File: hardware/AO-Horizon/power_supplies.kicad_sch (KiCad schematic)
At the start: 0 parts

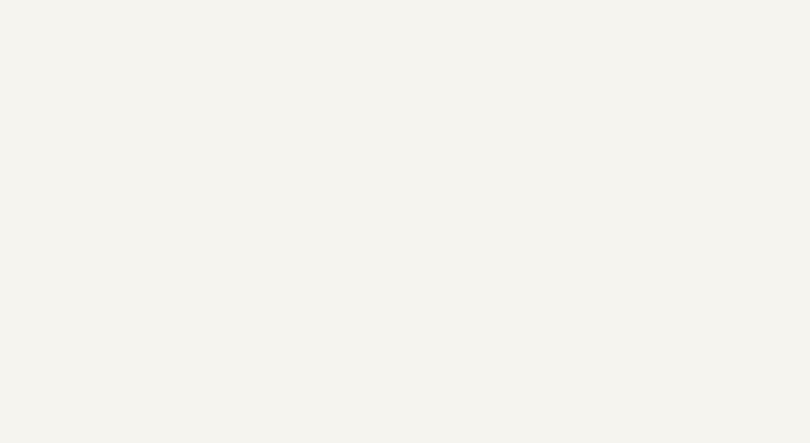
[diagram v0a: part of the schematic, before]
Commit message: feat(hardware): add project library, lib tables and design records (#4)
* docs(readme): simplify workflow diagram explanation

Mark DRAFT as under review, sync CHECK label, and add a colour key in README and template.

Co-Authored-By: Claude Sonnet 5.5 <noreply@anthropic.com>

* Update settings.json

* change spec file name

* update git-workflow skill

* change skill name by add hw-*

* docs: update AeroOptix-Horizon hardware spec

* docs: consolidate hardware handoff into checklist

* Update CLAUDE.md

* Update CLAUDE.md

* Update CLAUDE.md

* feat(hooks): replace protect hook with rule-based v2

Move file-protection rules into hooks/protect.json (allow > deny > ask)
and use ask for editable-with-approval files instead of a hard block.
Bash/PowerShell checks now inspect write targets, not any mention of a
protected path. Align settings.json permissions and drop the old hook.

Co-Authored-By: Claude Sonnet 5.5 <noreply@anthropic.com>

* docs: update CLAUDE.md for protection tiers and skill names

Describe the ask/deny protection rules, the v2 hook and protect.json,
and fix stale skill and template names.

Co-Authored-By: Claude Sonnet 5.5 <noreply@anthropic.com>

* Update .gitignore

* Update .gitignore

* Update .gitignore

* del skills

* Update engineering.md

* Update git-workflow.md

* Update hardware-workflow.md

* Update settings.json

* Update pull_request_template.md

* Update .gitignore

* Update .gitignore

* Delete SKILL.md

* Delete SKILL.md

* Update .gitignore

* add git-workflow skill

* Update CLAUDE.md

* Update protect.json

* Update settings.json

* Create MEMORY.md

* feat(agents): add codex-hw-delegate for bounded Codex tasks

Add a project agent that delegates one small, read-only-by-default task
to Codex CLI. It gates trivial or ambiguous requests, refuses PDF and
KiCad file contents, never mutates git, cross-checks Codex output and
returns a fixed report format.

Co-Authored-By: Claude Sonnet 5.5 <noreply@anthropic.com>

* fix(hooks): resol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
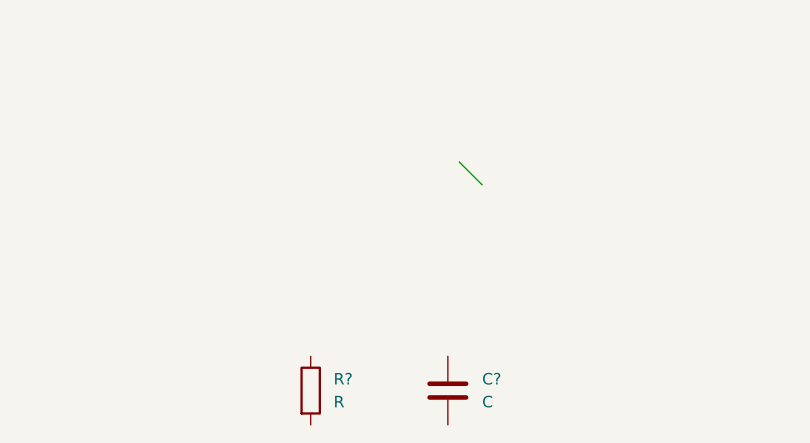
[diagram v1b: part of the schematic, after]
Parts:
- added C?: C, 0_Capacitor_SMD:C_0603_1608Metric_NomDensity, symbol Device:C
- added R?: R, 0_Resistor_SMD:R_0402_1005Metric_NomDensity, symbol Device:R
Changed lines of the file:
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@@
+		)
+	)
+	(bus_entry
+		(at 219.71 125.73)
+		(size 2.54 2.54)
+		(stroke
+			(width 0)
+			(type default)
+		)
+	)
+	(symbol
+		(lib_id "Device:C")
+		(at 218.44 151.13 0)
+		(unit 1)
+		(body_style 1)
+		(exclude_from_sim no)
+		(in_bom yes)
+		(on_board yes)
+		(in_pos_files yes)
+		(dnp no)
+		(fields_autoplaced yes)
+		(property "Reference" "C?"
+			(at 222.25 149.86 0)
+			(show_name no)
+			(do_not_autoplace no)
+			(effects
+				(font
+					(size 1.27 1.27)
+				)
+				(justify left)
+			)
+		)
+		(property "Value" "C"
+			(at 222.25 152.4 0)
+			(show_name no)
+			(do_not_autoplace no)
+			(effects
+				(font
+					(size 1.27 1.27)
+				)
+				(justify left)
+			)
+		)
+		(property "Footprint" "0_Capacitor_SMD:C_0603_1608Metric_NomDensity"
+			(at 219.4052 154.94 0)
+			(hide yes)
+			(show_name no)
+			(do_not_autoplace no)
+			(effects
+				(font
+					(size 1.27 1.27)
+				)
+			)
+		)
+		(property "Datasheet" ""
+			(at 218.44 151.13 0)
+			(hide yes)
+			(show_name no)
+			(do_not_autoplace no)
+			(effects
+				(font
+					(size 1.27 1.27)
+				)
+			)
+		)
+		(property "Description" "Unpolarized capacitor"
+			(at 218.44 151.13 0)
+			(hide yes)
+			(show_name no)
+			(do_not_autoplace no)
+			(effects
+				(font
+					(size 1.27 1.27)
+				)
+			)
+		)
+		(pin "1"
+		)
+		(pin "2"
+		)
+		(instances
+			(project "AO-Horizon"
+				(path "/76162bf1-0d95-48cb-b65a-4de551455d04/85f6b8f0-e85e-4d9f-8681-ac148f93be5a/5920cc04-6cd8-462c-b523-fb850d762b0c"
+					(reference "C?")
+					(unit 1)
+				)
+			)
+		)
+	)
+	(symbol
+		(lib_id "Device:R")
+		(at 203.2 151.13 0)
+		(unit 1)
+		(body_style 1)
+		(exclude_from_sim no)
+		(in_bom yes)
+		(on_board yes)
+		(in_pos_files yes)
+		(dnp no)
+		(fields_autoplaced yes)
+		(property "Reference" "R?"
+			(at 205.74 149.86 0)
+			(show_name no)
+			(do_not_autoplace no)
+			(effects
+				(font
+					(size 1.27 1.27)
+				)
+				(justify left)
+			)
+		)
+		(property "Value" "R"
+			(at 205.74 152.4 0)
+			(show_name no)
+			(do_not_autoplace no)
+			(effects
+				(font
+					(size 1.27 1.27)
+				)
+				(justify left)
+			)
+		)
+		(property "Footprint" "0_Resistor_SMD:R_0402_1005Metric_NomDensity"
+			(at 201.422 151.13 90)
+			(hide yes)
+			(show_name no)
+			(do_not_autoplace no)
+			(effects
+				(font
+					(size 1.27 1.27)
+				)
+			)
+		)
+		(property "Datasheet" ""
+			(at 203.2 151.13 0)
+			(hide yes)
+			(show_name no)
+			(do_not_autoplace no)
+			(effects
+				(font
+					(size 1.27 1.27)
+				)
+			)
+		)
+		(property "Description" "Resistor"
+			(at 203.2 151.13 0)
+			(hide yes)
+			(show_name no)
+			(do_not_autoplace no)
+			(effects
+				(font
+					(size 1.27 1.27)
+				)
+			)
+		)
+		(pin "2"
+		)
+		(pin "1"
+		)
+		(instances
+			(project "AO-Horizon"
+				(path "/76162bf1-0d95-48cb-b65a-4de551455d04/85f6b8f0-e85e-4d9f-8681-ac148f93be5a/5920cc04-6cd8-462c-b523-fb850d762b0c"
+					(reference "R?")
+					(unit 1)
+				)
+			)
 		)
 	)

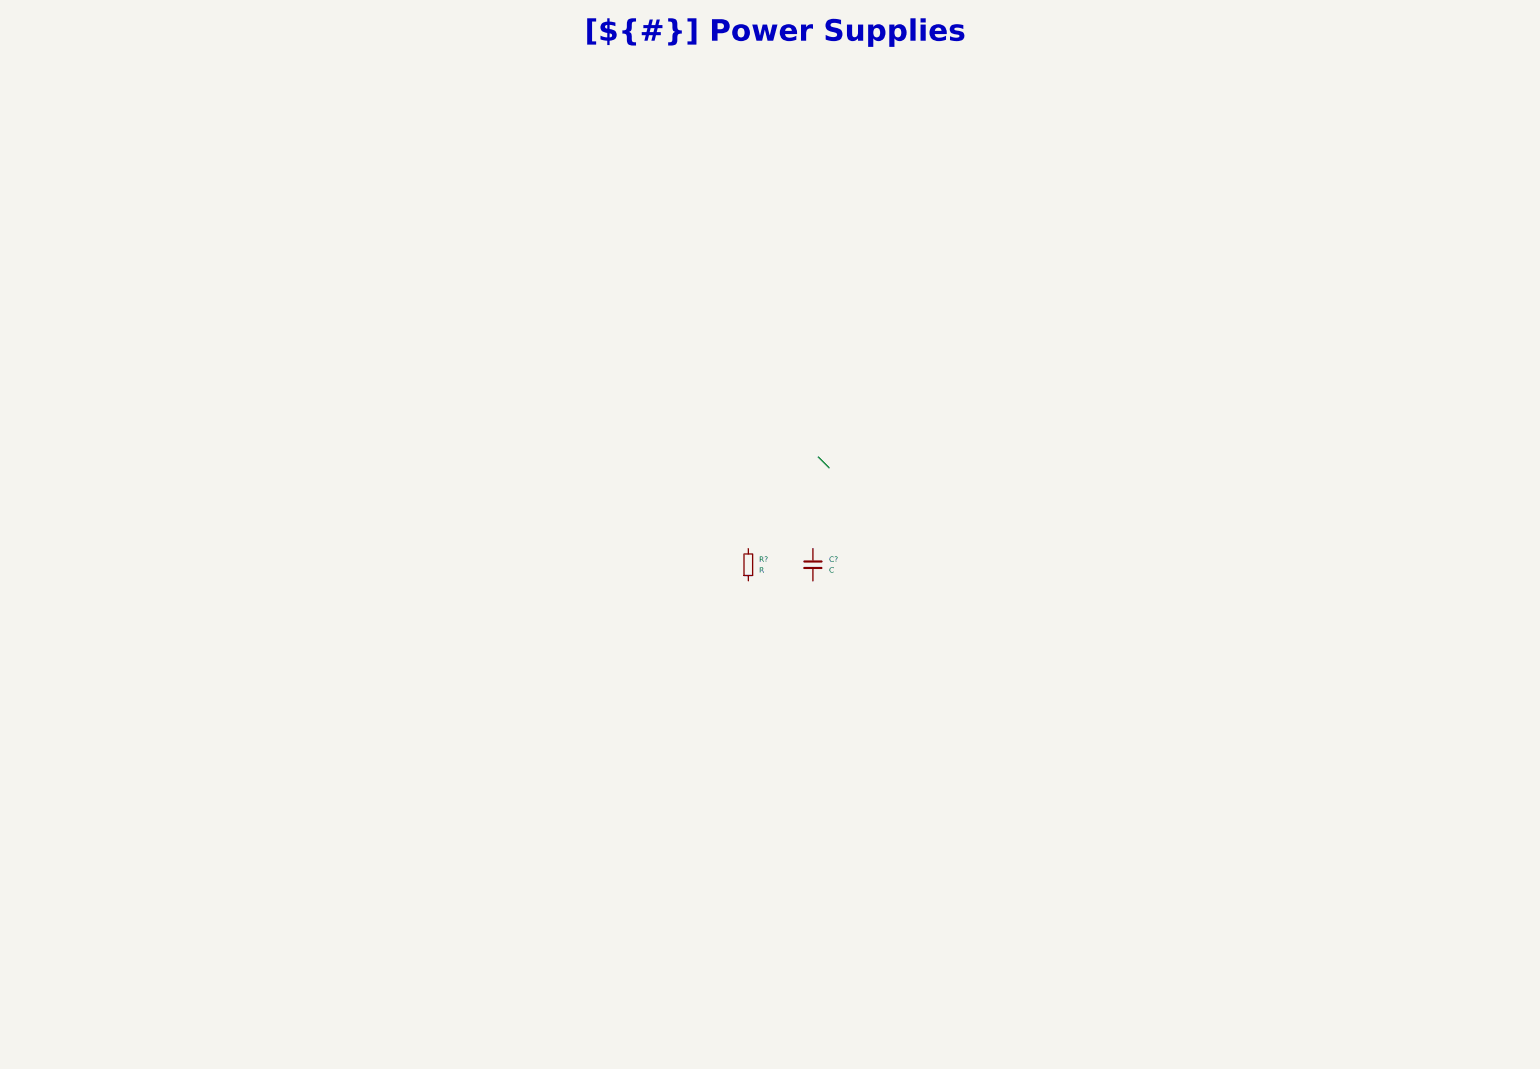
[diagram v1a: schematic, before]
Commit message: feat(power): add TPS62142 3V3 buck and power sheet parts
- power_supplies.kicad_sch: add TPS62142 buck (5V to 3V3) with inductor,
  capacitors and LED, TPS73533DRB LDO (+3.3VA), DF2S6.2CT ESD and a
  6-pin input connector.
- Add the new local libraries to fp-lib-table and sym-lib-table.
- Update AO-Horizon.kicad_sch (embedded font), block_diagram.kicad_sch
  and project settings.

ERC/DRC: NOT_VERIFIED.

Co-Authored-By: Claude Opus 5.5 <noreply@anthropic.com>
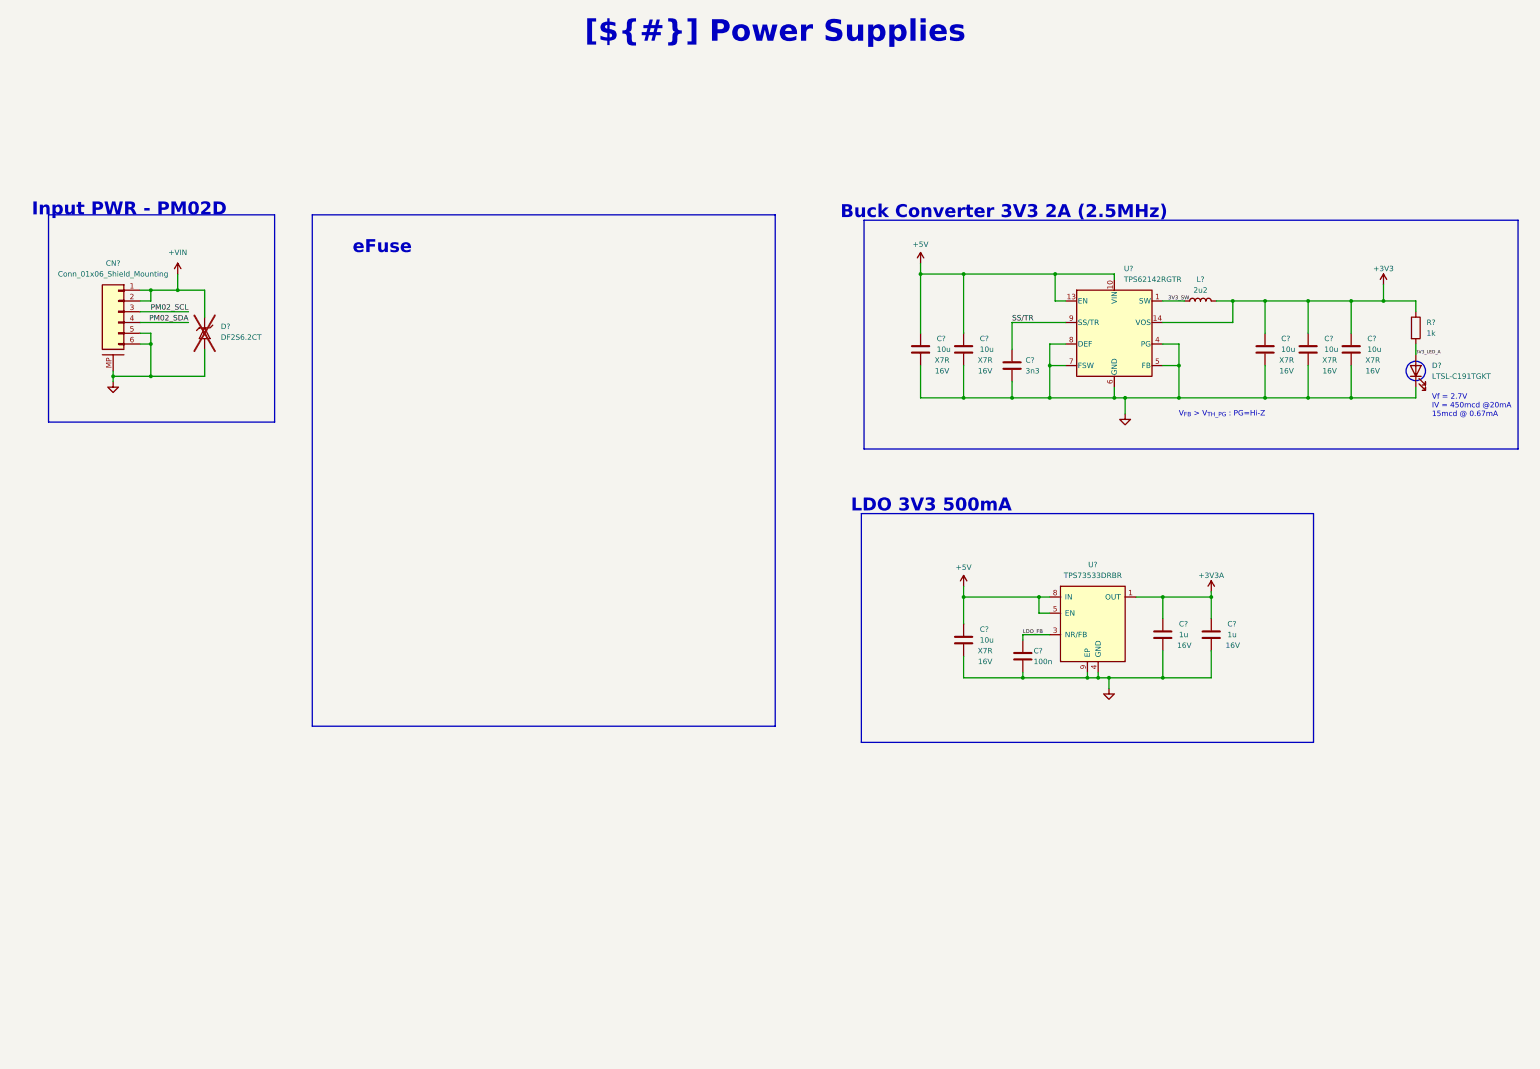
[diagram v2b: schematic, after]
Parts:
- removed C?: C, 0_Capacitor_SMD:C_0603_1608Metric_NomDensity, symbol Device:C
- removed R?: R, 0_Resistor_SMD:R_0402_1005Metric_NomDensity, symbol Device:R
- added C? (x2): 1u, 0_Capacitor_SMD:C_0603_1608Metric_NomDensity, symbol Device:C
- added C? (x6): 10u, 0_Capacitor_SMD:C_0805_2012Metric_NomDensity, symbol Device:C
- added C?: 3n3, 0_Capacitor_SMD:C_0603_1608Metric_NomDensity, symbol Device:C
- added C?: 100n, 0_Capacitor_SMD:C_0603_1608Metric_NomDensity, symbol Device:C
- added CN?: Conn_01x06_Shield_Mounting, 0_Conn_JST:JST_GH_SM06B-GHS-TB_1x06-1MP_P1.25mm_Horizontal, symbol 0_Conn_Generic:Conn_01x06_MountingPin
- added D?: LTSL-C191TGKT, 0_LED_SMD:LED_0603_1608Metric, symbol Device:LED
- added D?: DF2S6.2CT, 0_Diode_SMD:D_SOD-882, symbol 0_Protection_ESD:DF2S6.2CT
- added L?: 2u2, 0_Inductor_SMD:L_Abracon_AOTA-B252010S, symbol Device:L
- added R?: 1k, 0_Resistor_SMD:R_0603_1608Metric_NomDensity, symbol Device:R
- added U?: TPS73533DRBR, 0_Package_SON:VSON-8-1EP_3x3mm_P0.65mm__EP1.5x1.75mm_ThermalVias_DRV8601DRBT, symbol 0_Regulator_Linear:TPS73533DRB
- added U?: TPS62142RGTR, 0_Package_DFN_QFN:VQFN-16-1EP_3x3mm_P0.5mm_EP1.68x1.68mm_ThermalVias, symbol 0_Regulator_Switching:TPS62142
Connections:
- new net +3V3: C?.1, C?.1, C?.1, L?.2, R?.1, U?.14 (VOS)
- new net +3V3A: C?.1, C?.1, U?.1 (OUT)
- new net +5V: C?.1, C?.1, C?.1, U?.10 (VIN), U?.11 (VIN), U?.12 (VIN), U?.13 (EN), U?.5 (EN), U?.8 (IN)
- new net +VIN: CN?.1 (Pin_1), CN?.2 (Pin_2), D?.1
- new net 3V3_LED_A: D?.2 (A), R?.2
- new net 3V3_SW: L?.1, U?.1 (SW), U?.2 (SW), U?.3 (SW)
- new net GND: C?.2, C?.2, C?.2, C?.2, C?.2, C?.2, C?.2, C?.2, C?.2, C?.2, CN?.5 (Pin_5), CN?.6 (Pin_6), CN?.MP (MountPin), D?.1 (K), D?.2, U?.15 (GND), U?.16 (GND), U?.17 (GND), U?.4 (GND), U?.4 (PG), U?.5 (FB), U?.6 (GND), U?.7 (FSW), U?.8 (DEF), U?.9 (EP)
- new net LDO_FB: C?.1, U?.3 (NR/FB)
- new net PM02_SCL: CN?.3 (Pin_3)
- new net PM02_SDA: CN?.4 (Pin_4)
- new net SS/TR: C?.1, U?.9 (SS/TR)
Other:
- note added: "Buck Converter 3V3 2A (2.5MHz)"
- note added: "Input PWR - PM02D"
- note added: "LDO 3V3 500mA"
- note added: "V_{FB} > V_{TH_PG} : PG=Hi-Z"
- note added: "Vf = 2.7V IV = 450mcd @20mA 15mcd @ 0.67mA"
- note added: "eFuse"

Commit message: feat(library): add sensor starting points and sync design docs (#8)
* docs(readme): simplify workflow diagram explanation

Mark DRAFT as under review, sync CHECK label, and add a colour key in README and template.

Co-Authored-By: Claude Sonnet 5.5 <noreply@anthropic.com>

* Update settings.json

* change spec file name

* update git-workflow skill

* change skill name by add hw-*

* docs: update AeroOptix-Horizon hardware spec

* docs: consolidate hardware handoff into checklist

* Update CLAUDE.md

* Update CLAUDE.md

* Update CLAUDE.md

* feat(hooks): replace protect hook with rule-based v2

Move file-protection rules into hooks/protect.json (allow > deny > ask)
and use ask for editable-with-approval files instead of a hard block.
Bash/PowerShell checks now inspect write targets, not any mention of a
protected path. Align settings.json permissions and drop the old hook.

Co-Authored-By: Claude Sonnet 5.5 <noreply@anthropic.com>

* docs: update CLAUDE.md for protection tiers and skill names

Describe the ask/deny protection rules, the v2 hook and protect.json,
and fix stale skill and template names.

Co-Authored-By: Claude Sonnet 5.5 <noreply@anthropic.com>

* Update .gitignore

* Update .gitignore

* Update .gitignore

* del skills

* Update engineering.md

* Update git-workflow.md

* Update hardware-workflow.md

* Update settings.json

* Update pull_request_template.md

* Update .gitignore

* Update .gitignore

* Delete SKILL.md

* Delete SKILL.md

* Update .gitignore

* add git-workflow skill

* Update CLAUDE.md

* Update protect.json

* Update settings.json

* Create MEMORY.md

* feat(agents): add codex-hw-delegate for bounded Codex tasks

Add a project agent that delegates one small, read-only-by-default task
to Codex CLI. It gates trivial or ambiguous requests, refuses PDF and
KiCad file contents, never mutates git, cross-checks Codex output and
returns a fixed report format.

Co-Authored-By: Claude Sonnet 5.5 <noreply@anthropic.com>

* fix(hooks): resolve .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
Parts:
- U?: footprint 0_Package_SON:VSON-8-1EP_3x3mm_P0.65mm__EP1.5x1.75mm_ThermalVias_DRV8601DRBT -> 0_Package_SON:VSON-8-1EP_3x3mm_P0.65mm_EP1.5x1.75mm_ThermalVias
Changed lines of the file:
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@@
 			)
 		)
-		(property "Footprint" "0_Package_SON:VSON-8-1EP_3x3mm_P0.65mm__EP1.5x1.75mm_ThermalVias_DRV8601DRBT"
+		(property "Footprint" "0_Package_SON:VSON-8-1EP_3x3mm_P0.65mm_EP1.5x1.75mm_ThermalVias"
 			(at 283.21 147.32 0)
 			(hide yes)
